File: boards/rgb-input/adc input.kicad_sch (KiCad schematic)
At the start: 4 parts, among them J10 Conn_01x03

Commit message: this board is going to be sick.
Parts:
- renumbered C12 to C3, R19 to R17

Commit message: tested the bus voltage stuff a bit more
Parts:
- renumbered C3 to C11, R17 to R19

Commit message: some adc changes and then rerouting
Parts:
- renumbered C11 to C3, R19 to R17

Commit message: figured out most of the components, working on placement
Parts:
- ADC0: renamed from J10; value Conn_01x03 -> ~; footprint (none) -> Connector_JST:JST_PH_B3B-PH-K_1x03_P2.00mm_Vertical
- renumbered C3 to C12, R17 to R1

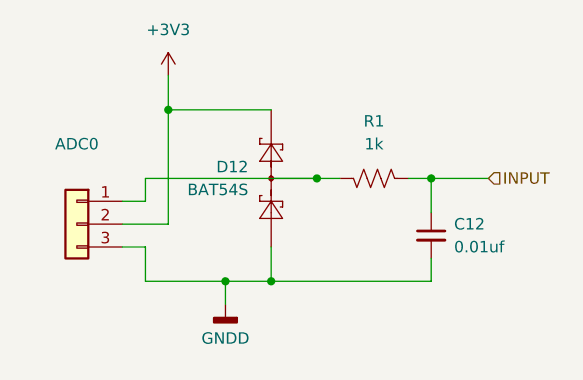
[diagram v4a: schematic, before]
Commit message: more layout checks on the input board
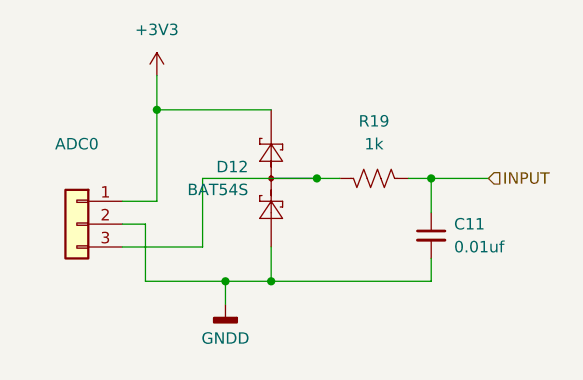
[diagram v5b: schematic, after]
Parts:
- renumbered C12 to C11, R1 to R19
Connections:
- net +3V3: now also ADC0.1 (Pin_1); no longer ADC0.2 (Pin_2)
- net GNDD: now also ADC0.2 (Pin_2); no longer ADC0.3 (Pin_3)
- net at D12.3 (COM), R19.1: now also ADC0.3 (Pin_3); no longer ADC0.1 (Pin_1)

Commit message: routed the rgb setup
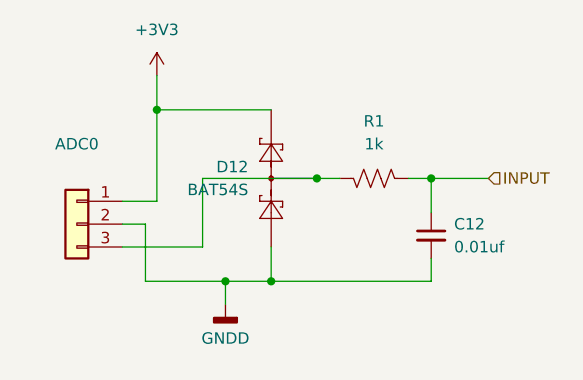
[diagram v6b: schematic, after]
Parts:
- renumbered C11 to C12, R19 to R1

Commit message: so much routing.
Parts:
- renumbered C12 to C3, R1 to R17

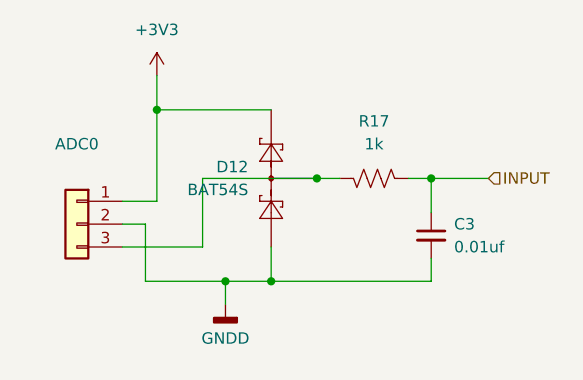
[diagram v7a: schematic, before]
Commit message: whoa, board is fully routed!!!!
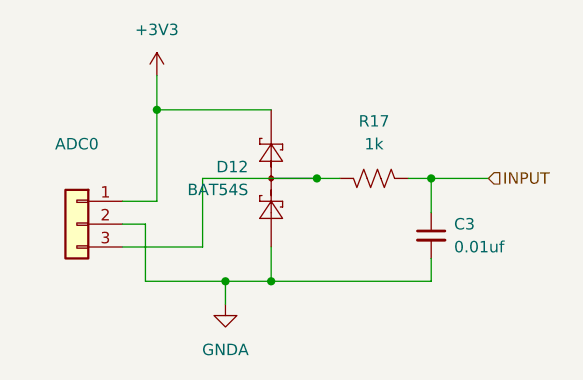
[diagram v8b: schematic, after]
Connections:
- net GNDD renamed GNDA
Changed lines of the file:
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@@
+    )
+  )
+  (symbol (lib_id "power:GNDA") (at 139.7 104.14 0) (unit 1)
+    (in_bom yes) (on_board yes) (dnp no) (fields_autoplaced)
+    (property "Reference" "#PWR032" (at 139.7 110.49 0)
+      (effects (font (size 1.27 1.27)) hide)
+    )
+    (property "Value" "GNDA" (at 139.7 109.22 0)
+      (effects (font (size 1.27 1.27)))
+    )
+    (property "Footprint" "" (at 139.7 104.14 0)
+      (effects (font (size 1.27 1.27)) hide)
+    )
+    (property "Datasheet" "" (at 139.7 104.14 0)
+      (effects (font (size 1.27 1.27)) hide)
+    )
+    (pin "1")
+    (instances
+      (project "rgb-input"
+        (path "/c83c6236-96e9-46ad-9d7a-9e2efa4a7966/c9e1b2da-9064-45a5-a0a2-ee072f7e1acf"
+          (reference "#PWR032") (unit 1)
+        )
+        (path "/c83c6236-96e9-46ad-9d7a-9e2efa4a7966/120468c6-3bec-414c-9049-57af589f397a"
+          (reference "#PWR027") (unit 1)
+        )
+        (path "/c83c6236-96e9-46ad-9d7a-9e2efa4a7966/f06c9bf0-de4e-49a2-91ec-1c9426377826"
+          (reference "#PWR030") (unit 1)
+        )
+        (path "/c83c6236-96e9-46ad-9d7a-9e2efa4a7966/1ca70e91-4481-4c96-8c08-39dd142498e5"
+          (reference "#PWR034") (unit 1)
+        )
+        (path "/c83c6236-96e9-46ad-9d7a-9e2efa4a7966/597c781a-3a73-4808-b6ed-8c917478e623"
+          (reference "#PWR036") (unit 1)
+        )
+        (path "/c83c6236-96e9-46ad-9d7a-9e2efa4a7966/7fda9512-7a31-4b6e-85db-2478bfe7f375"
+          (reference "#PWR038") (unit 1)
+        )
+        (path "/c83c6236-96e9-46ad-9d7a-9e2efa4a7966/d24c7443-0875-4d8e-b56e-81b211cd6f3d"
+          (reference "#PWR040") (unit 1)
+        )
+        (path "/c83c6236-96e9-46ad-9d7a-9e2efa4a7966/76149826-8526-4a6c-8e11-6dc0109cc281"
+          (reference "#PWR042") (unit 1)
+        )
+      )
     )
   )
@@
         )
       )
-    )
-  )
-  (symbol (lib_id "power:GNDD") (at 139.7 104.14 0) (mirror y) (unit 1)
-    (in_bom yes) (on_board yes) (dnp no) (fields_autoplaced)
-    (property "Reference" "#PWR03" (at 139.7 110.49 0)
-      (effects (font (size 1.27 1.27)) hide)
-    )
-    (property "Value" "GNDD" (at 139.7 107.95 0)
-      (effects (font (size 1.27 1.27)))
-    )
-    (property "Footprint" "" (at 139.7 104.14 0)
-      (effects (font (size 1.27 1.27)) hide)
-    )
-    (property "Datasheet" "" (at 139.7 104.14 0)
-      (effects (font (size 1.27 1.27)) hide)
-    )
-    (pin "1")
-    (instances
-      (project "rgb-input"
-        (path "/c83c6236-96e9-46ad-9d7a-9e2efa4a7966/ef548cdc-9d5d-4f8e-8f54-0c2e96dbe3f0"
-          (reference "#PWR03") (unit 1)
-        )
-        (path "/c83c6236-96e9-46ad-9d7a-9e2efa4a7966/76149826-8526-4a6c-8e11-6dc0109cc281"
-          (reference "#PWR042") (unit 1)
-        )
-        (path "/c83c6236-96e9-46ad-9d7a-9e2efa4a7966/d24c7443-0875-4d8e-b56e-81b211cd6f3d"
-          (reference "#PWR040") (unit 1)
-        )
-        (path "/c83c6236-96e9-46ad-9d7a-9e2efa4a7966/7fda9512-7a31-4b6e-85db-2478bfe7f375"
-          (reference "#PWR038") (unit 1)
-        )
-        (path "/c83c6236-96e9-46ad-9d7a-9e2efa4a7966/597c781a-3a73-4808-b6ed-8c917478e623"
-          (reference "#PWR036") (unit 1)
-        )
-        (path "/c83c6236-96e9-46ad-9d7a-9e2efa4a7966/1ca70e91-4481-4c96-8c08-39dd142498e5"
-          (reference "#PWR034") (unit 1)
-        )
-        (path "/c83c6236-96e9-46ad-9d7a-9e2efa4a7966/c9e1b2da-9064-45a5-a0a2-ee072f7e1acf"
-          (reference "#PWR032") (unit 1)
-        )
-        (path "/c83c6236-96e9-46ad-9d7a-9e2efa4a7966/120468c6-3bec-414c-9049-57af589f397a"
-          (reference "#PWR030") (unit 1)
-        )
-        (path "/c83c6236-96e9-46ad-9d7a-9e2efa4a7966/a581b924-afd8-4b56-b69e-790286072066"
-          (reference "#PWR025") (unit 1)
-        )
-        (path "/c83c6236-96e9-46ad-9d7a-9e2efa4a7966/f06c9bf0-de4e-49a2-91ec-1c9426377826"
-          (reference "#PWR027") (unit 1)
-        )
-        (path "/c83c6236-96e9-46ad-9d7a-9e2efa4a7966/803edf1a-5825-4947-a8b9-85d3a29697e5"
-          (reference "#PWR023") (unit 1)
-        )
-        (path "/c83c6236-96e9-46ad-9d7a-9e2efa4a7966/802175d5-fb4b-4457-a117-b0f397189ff7"
-          (reference "#PWR021") (unit 1)
-        )
-        (path "/c83c6236-96e9-46ad-9d7a-9e2efa4a7966/5fc618b8-7830-4bbf-bf46-7753631e9b1e"
-          (reference "#PWR019") (unit 1)
-        )
-        (path "/c83c6236-96e9-46ad-9d7a-9e2efa4a7966/145fa34f-e19e-43e2-bb48-aff2e824ef0a"
-          (reference "#PWR017") (unit 1)
-        )
-        (path "/c83c6236-96e9-46ad-9d7a-9e2efa4a7966/6f6f2d8d-82f6-4691-bba7-8caa1bd52e96"
-          (reference "#PWR015") (unit 1)
-        )
-        (path "/c83c6236-96e9-46ad-9d7a-9e2efa4a7966/4175a172-5c0b-4d6a-88bb-129f5f07b813"
-          (reference "#PWR013") (unit 1)
-        )
-        (path "/c83c6236-96e9-46ad-9d7a-9e2efa4a7966/4f50afed-9381-4977-8e27-209f0f88ad4e"
-          (reference "#PWR08") (unit 1)
-        )
-      )
